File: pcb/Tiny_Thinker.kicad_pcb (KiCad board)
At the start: 4 copper layers, 65 x 63.1 mm, 43 parts, among them J2 PERIPHERALS, J3 ADC_TIM, J8 USB_C_Receptacle_USB2.0_16P, SW1 SW_Push, SW2 SW_SPDT, U1 STM32F446RET6, U2 AMS1117-3.3, Y1 16MHz

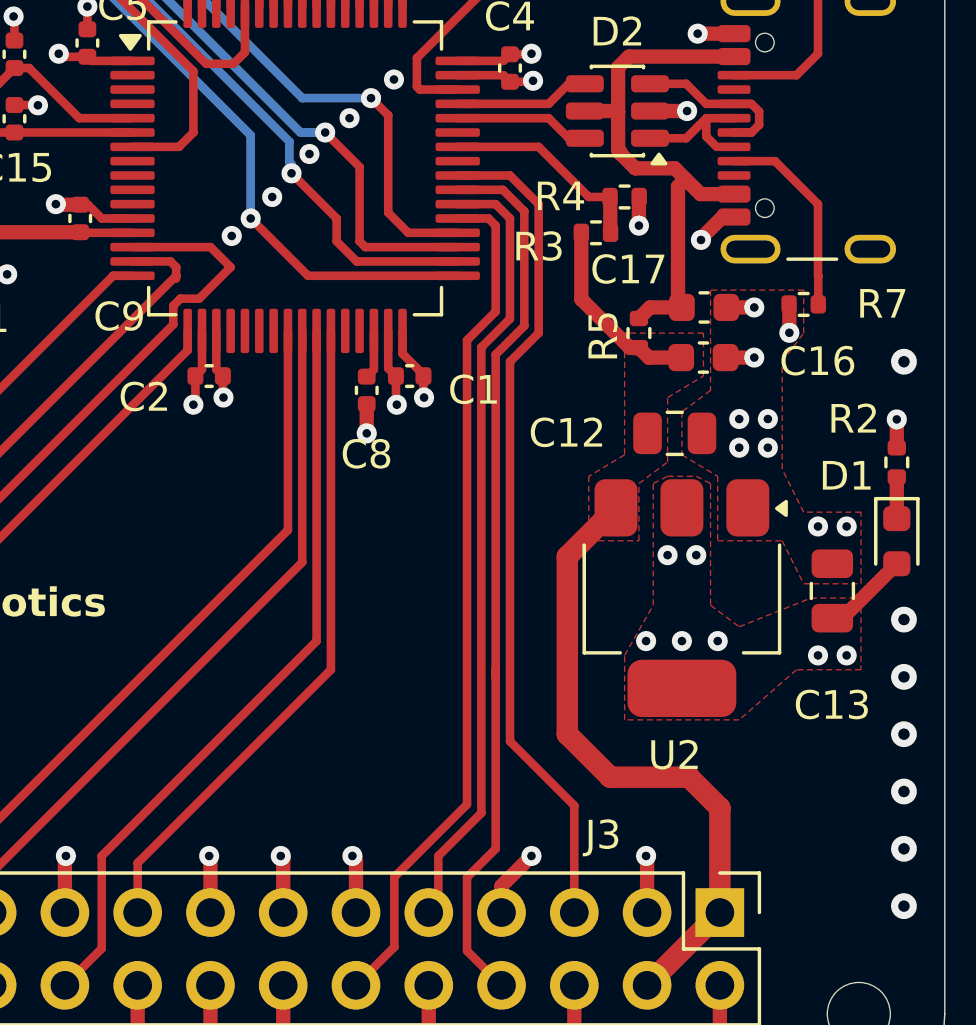
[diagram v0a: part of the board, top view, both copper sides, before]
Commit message: Revised JLCPCB capabilities
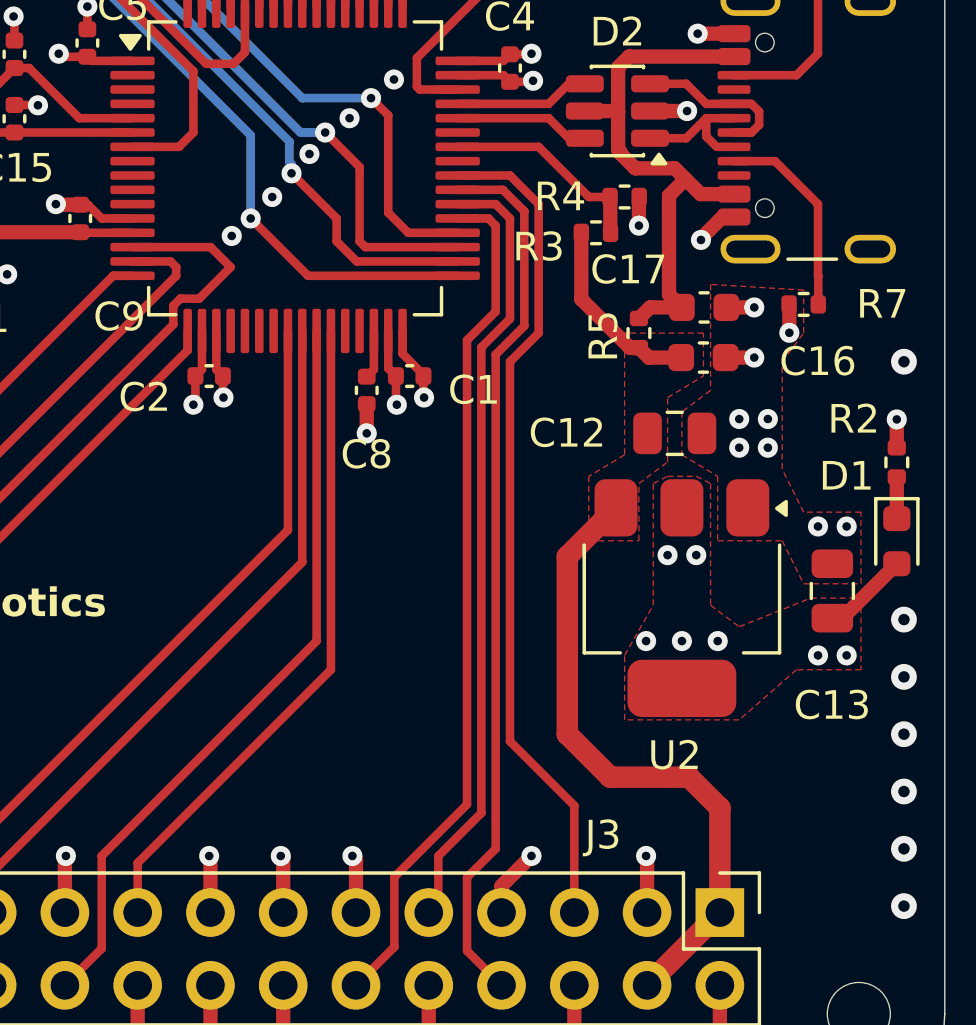
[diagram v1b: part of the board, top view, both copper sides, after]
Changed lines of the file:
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@@
-	)
-	(segment
-		(start 150.114 105.969)
-		(end 150.114 101.886)
-		(width 0.5)
-		(layer "F.Cu")
-		(net 21)
 	)
 	(segment
@@
 	)
 	(segment
+		(start 150.25 106.105)
+		(end 149.8 105.655)
+		(width 0.5)
+		(layer "F.Cu")
+		(net 21)
+	)
+	(segment
 		(start 150.75 102)
 		(end 150.375 101.625)
@@
 	)
 	(segment
+		(start 149.8 105.655)
+		(end 149.8 102.2)
+		(width 0.5)
+		(layer "F.Cu")
+		(net 21)
+	)
+	(segment
 		(start 147.999 99.25)
 		(end 148.024 99.275)
@@
 	)
 	(segment
-		(start 150.25 106.105)
-		(end 150.114 105.969)
+		(start 149.8 102.2)
+		(end 150.375 101.625)
 		(width 0.5)
 		(layer "F.Cu")
@@
 	)
 	(segment
-		(start 150.114 101.886)
-		(end 150.375 101.625)
-		(width 0.5)
-		(layer "F.Cu")
-		(net 21)
-	)
-	(segment
 		(start 148.024 99.275)
 		(end 148.024 97.726)
@@
 	)
 	(segment
-		(start 132.6 105)
-		(end 132.6 105.1)
-		(width 0.3)
-		(layer "F.Cu")
-		(net 25)
-	)
-	(segment
 		(start 131.075 104.5)
 		(end 132.4 104.5)
@@
 	)
 	(segment
+		(start 144.75 102.75)
+		(end 144.75 106.75)
+		(width 0.3)
+		(layer "F.Cu")
+		(net 34)
+	)
+	(segment
+		(start 142.75 128.56)
+		(end 143.955 129.765)
+		(width 0.3)
+		(layer "F.Cu")
+		(net 34)
+	)
+	(segment
+		(start 143.75 107.75)
+		(end 143.75 125)
+		(width 0.3)
+		(layer "F.Cu")
+		(net 34)
+	)
+	(segment
+		(start 144.75 106.75)
+		(end 143.75 107.75)
+		(width 0.3)
+		(layer "F.Cu")
+		(net 34)
+	)
+	(segment
+		(start 143.75 125)
+		(end 142.75 126)
+		(width 0.3)
+		(layer "F.Cu")
+		(net 34)
+	)
+	(segment
 		(start 142.425 102)
 		(end 144 102)
@@
 	)
 	(segment
-		(start 142.75 128.56)
-		(end 143.955 129.765)
+		(start 142.75 126)
+		(end 142.75 128.56)
 		(width 0.3)
 		(layer "F.Cu")
@@
 		(start 144 102)
 		(end 144.75 102.75)
-		(width 0.3)
-		(layer "F.Cu")
-		(net 34)
-	)
-	(segment
-		(start 143.75 119)
-		(end 143.75 118.75)
-		(width 0.3)
-		(layer "F.Cu")
-		(net 34)
-	)
-	(segment
-		(start 143.75 125)
-		(end 142.75 126)
-		(width 0.3)
-		(layer "F.Cu")
-		(net 34)
-	)
-	(segment
-		(start 143.75 119)
-		(end 143.75 125)
-		(width 0.3)
-		(layer "F.Cu")
-		(net 34)
-	)
-	(segment
-		(start 144.75 102.75)
-		(end 144.75 106.75)
-		(width 0.3)
-		(layer "F.Cu")
-		(net 34)
-	)
-	(segment
-		(start 143.75 107.75)
-		(end 143.75 119)
-		(width 0.3)
-		(layer "F.Cu")
-		(net 34)
-	)
-	(segment
-		(start 142.75 126)
-		(end 142.75 128.56)
-		(width 0.3)
-		(layer "F.Cu")
-		(net 34)
-	)
-	(segment
-		(start 144.75 106.75)
-		(end 143.75 107.75)
 		(width 0.3)
 		(layer "F.Cu")
@@
 		(min_thickness 0.25)
 		(filled_areas_thickness no)
-		(fill yes
+		(fill
 			(thermal_gap 0.3)
 			(thermal_bridge_width 0.3)
@@
 			(pts
 				(xy 151.5 114.25) (xy 153.75 114.25) (xy 154.5 115.75) (xy 156.5 115.75) (xy 156.5 113.25) (xy 154.5 113.25)
-				(xy 153.75 111.75) (xy 153.75 108) (xy 154.5 107) (xy 154.5 105.5) (xy 151.25 105.5) (xy 151.25 109)
+				(xy 153.75 111.75) (xy 153.75 108) (xy 154.5 107) (xy 154.5 105.5) (xy 151.25 105.3) (xy 151.25 109)
 				(xy 150.25 109.75) (xy 150.25 111.25) (xy 151.5 112)
 			)

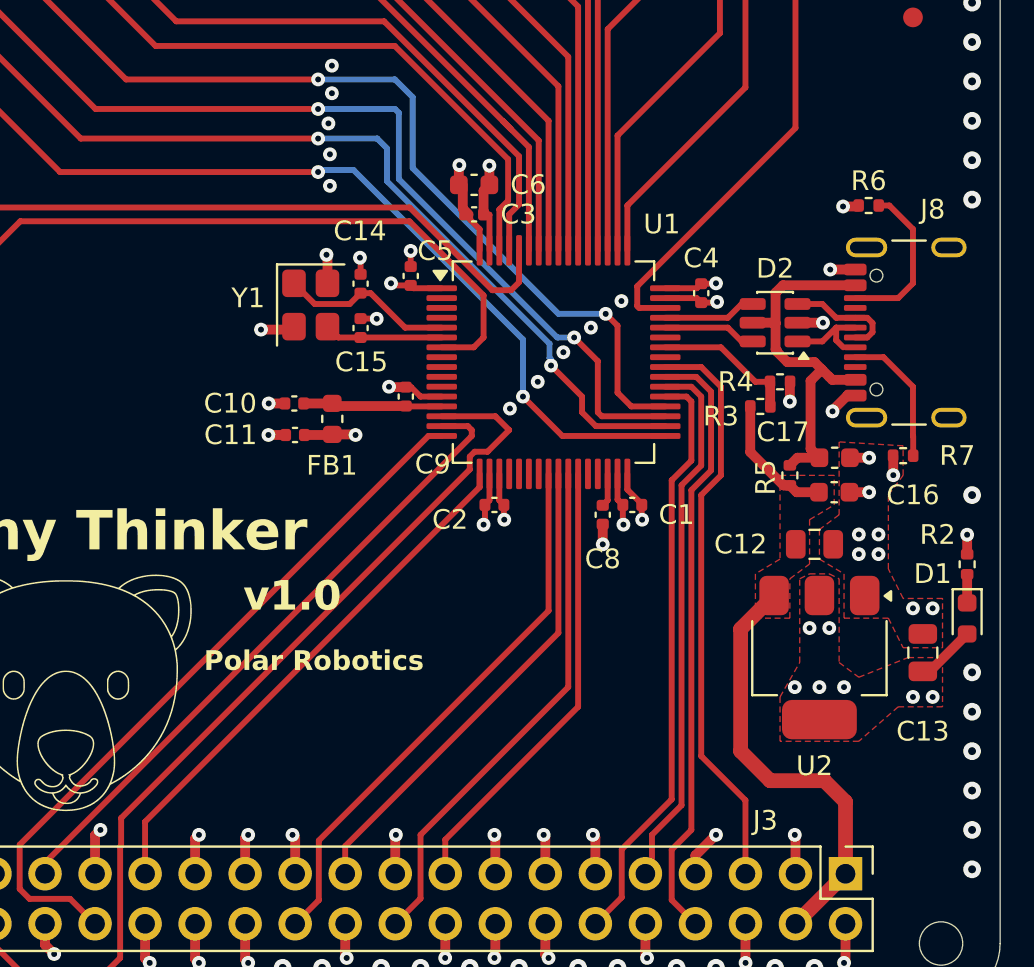
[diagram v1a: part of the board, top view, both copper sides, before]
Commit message: cleaned up routing of USB data lines
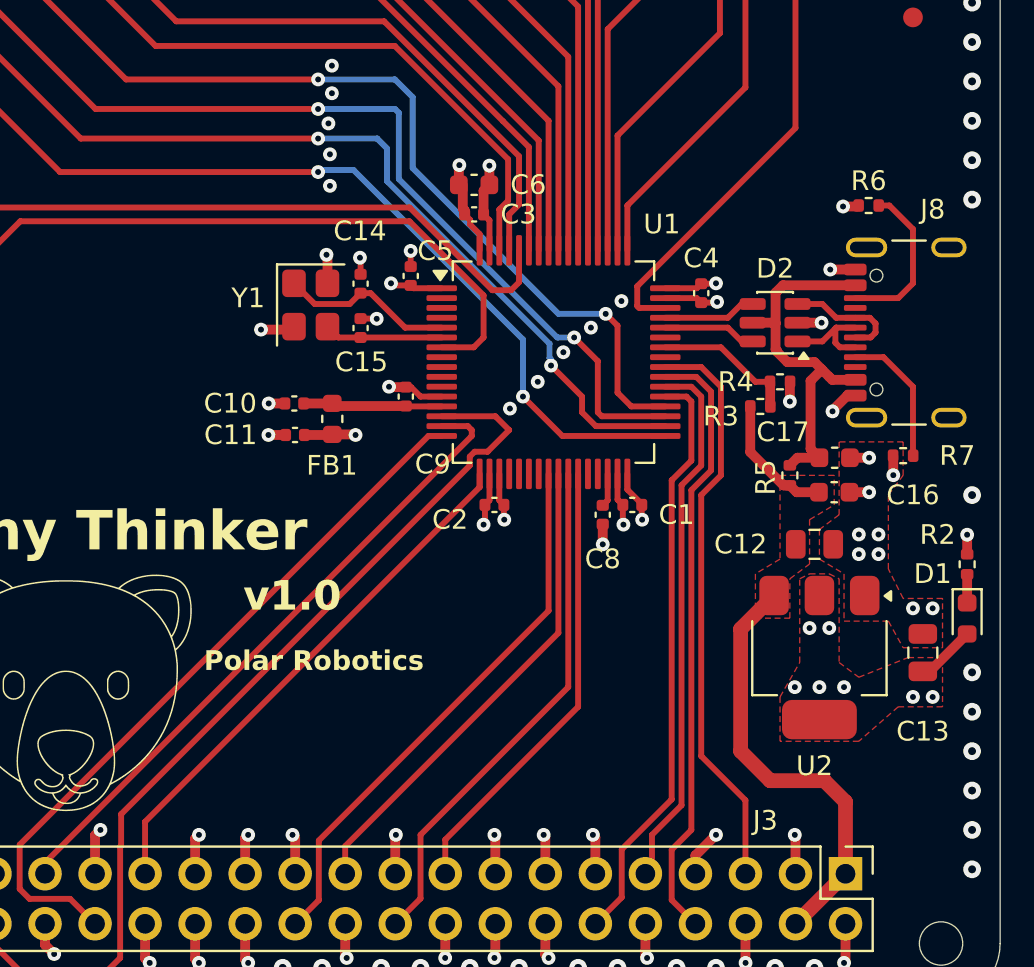
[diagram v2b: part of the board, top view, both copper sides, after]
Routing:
- net /I2C1_SDA: track 28.2 -> 27.6 mm

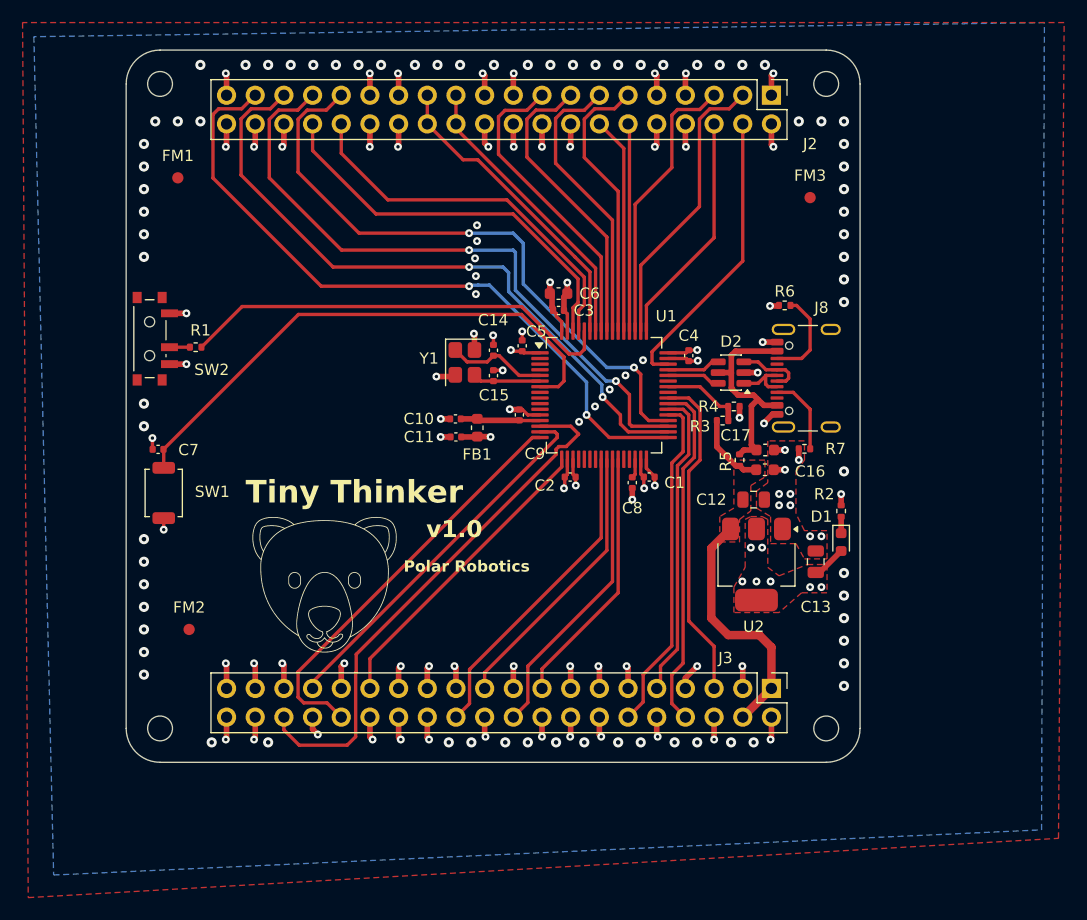
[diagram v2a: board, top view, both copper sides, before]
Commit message: changed header routing to be more spaced out
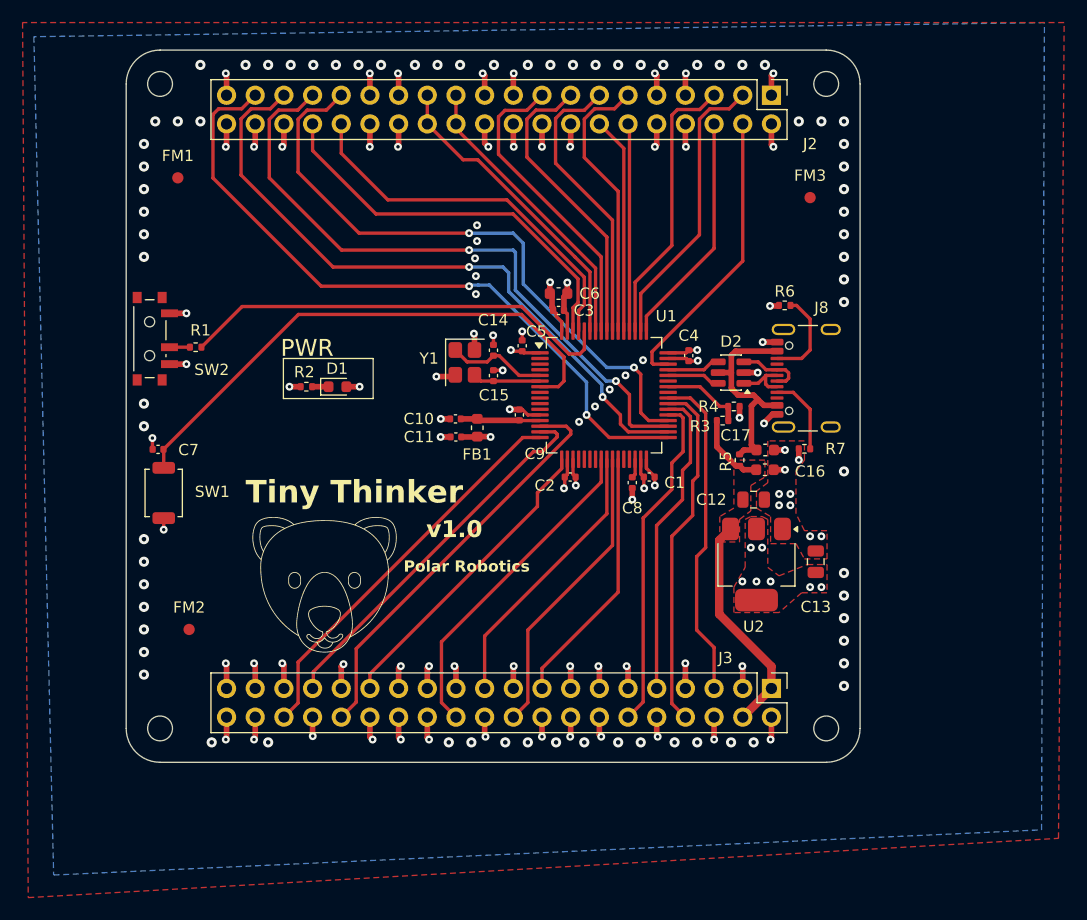
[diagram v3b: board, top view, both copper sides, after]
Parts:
- moved R2 48.6 mm to (110.4, 100.5), turned to 180 degrees
- moved D1 46.7 mm to (113.1, 100.5), turned to 0 degrees
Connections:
- D2 pad 1: /USB_D- -> /USB__CONN_D-
- D2 pad 3: /USB_D+ -> /USB__CONN_D+
- J3 pad 32: /TIM2_CH3 -> /TIM2_CH1
- J3 pad 36: /TIM2_CH1 -> /TIM2_CH3
- J8 pad A6: /USB_D+ -> /USB__CONN_D+
- J8 pad A7: /USB_D- -> /USB__CONN_D-
- J8 pad B6: /USB_D+ -> /USB__CONN_D+
- J8 pad B7: /USB_D- -> /USB__CONN_D-
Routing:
- net /TIM2_CH1: track 47.4 -> 36.7 mm
- net /USB_D+: track 10.7 -> 4.73 mm
- net /USB__CONN_D+: track 0.00 -> 5.97 mm
- net /USB__CONN_D-: track 0.00 -> 5.12 mm
- net /USB_D-: track 9.84 -> 4.73 mm
- net +VBUSF: track 28.9 -> 26.7 mm
- net /TIM2_CH3: track 36.8 -> 35.1 mm
- net +3.3V: track 54.9 -> 53.4 mm, vias 30 -> 31
- net /ADC1_IN14: track 28.2 -> 29.2 mm
- net GND: track 97.7 -> 98.3 mm
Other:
- board text added: "PWR"

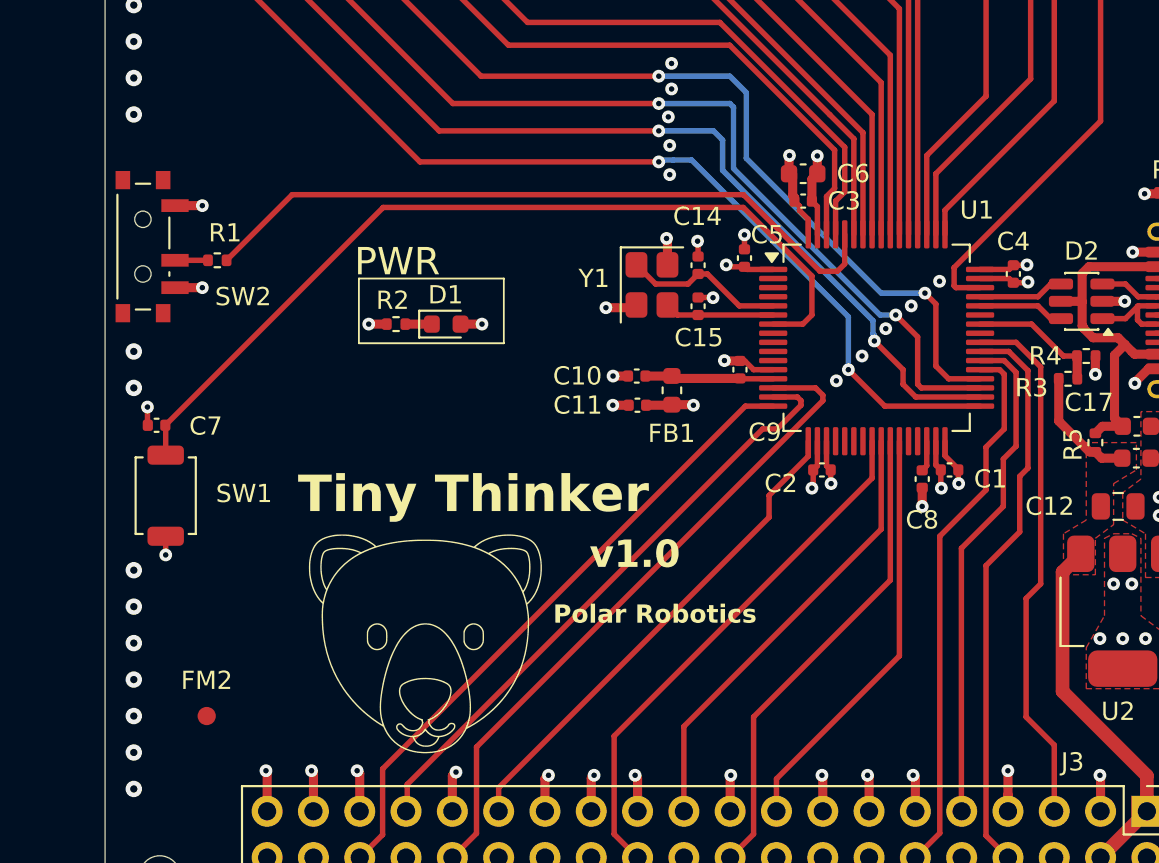
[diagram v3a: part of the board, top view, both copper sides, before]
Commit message: Added user led
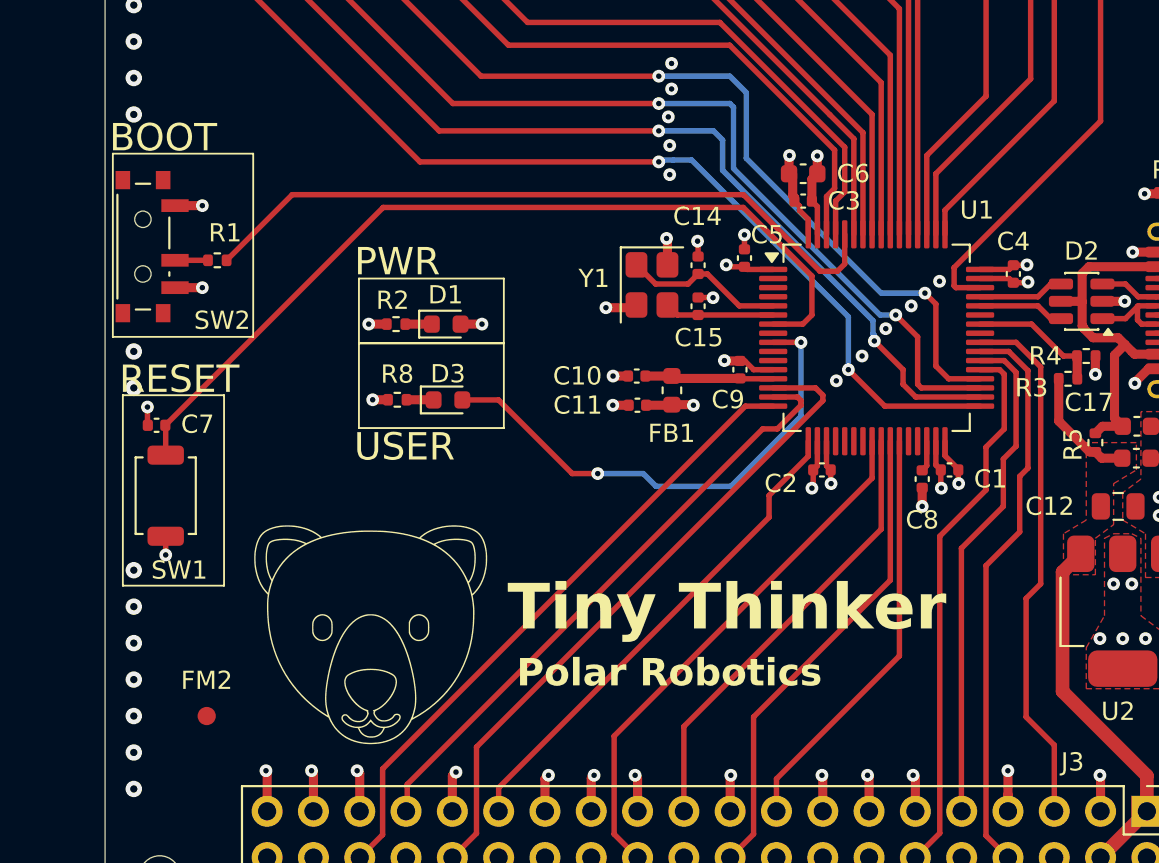
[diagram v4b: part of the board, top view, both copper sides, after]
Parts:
- added D3: BLUE, LED_SMD:LED_0603_1608Metric, F.Cu at (113.2, 104.7)
- added R8: 1k5, Resistor_SMD:R_0402_1005Metric, F.Cu at (110.5, 104.7)
- moved G*** 3.04 mm to (109.0, 117.5)
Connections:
- U1 pad 9: unconnected-(U1-PC1-Pad9) -> /GPIO_USER_LED
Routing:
- net /GPIO_USER_LED: track 0.00 -> 27.7 mm, vias 0 -> 2
- net /USER_LED_K: track 0.00 -> 1.49 mm
- net GND: track 98.3 -> 99.2 mm, vias 144 -> 145
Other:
- board text added: "02/2026"
- board text added: "BOOT"
- board text added: "RESET"
- board text added: "Rev 1.0"
- board text added: "USER"
- board text removed: "v1.0"

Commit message: cleaned up routing
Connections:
- net /GPIO_USER_LED renamed /GPIO_USER_LED_B
- net /USER_LED_K renamed /USER_LED_B_K
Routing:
- net /GPIO_USER_LED_B: track 27.7 -> 28.4 mm
- net GND: vias 145 -> 147
